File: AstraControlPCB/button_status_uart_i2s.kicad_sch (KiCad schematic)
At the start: 17 parts, among them CN7 4P JST ZH, CN8 4P JST ZH, CN9 JST_ZH_6PIN_1A_250V

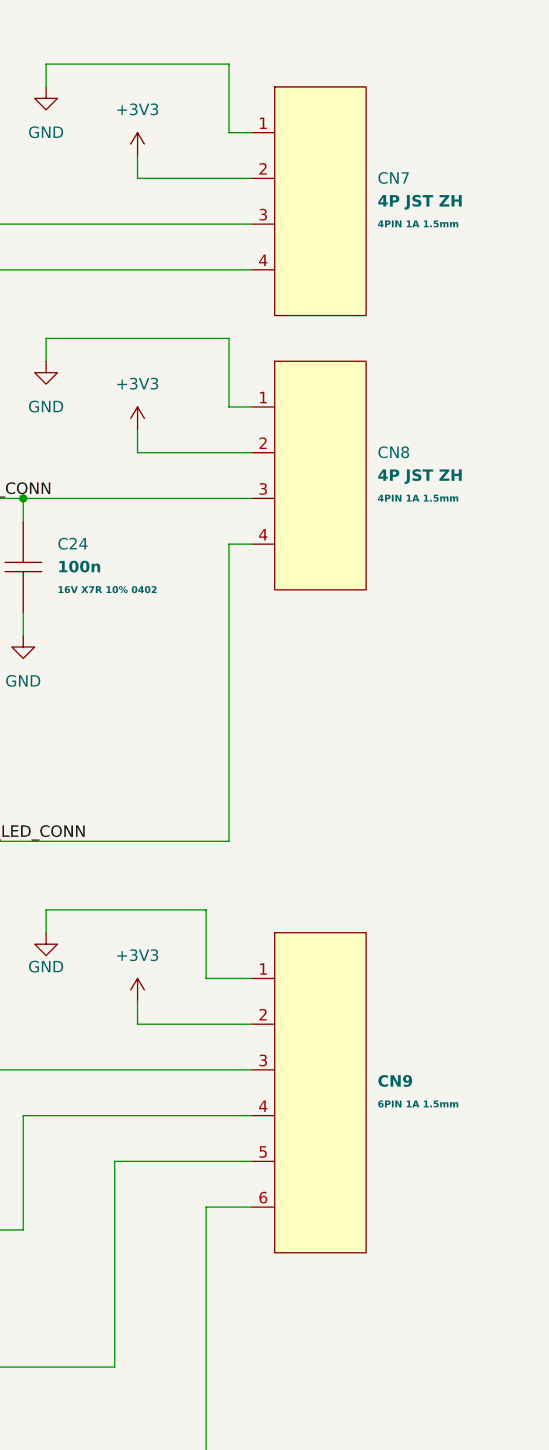
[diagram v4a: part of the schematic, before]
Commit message: Updated to JST SH, 3A diode for USB, added extra 2P VH
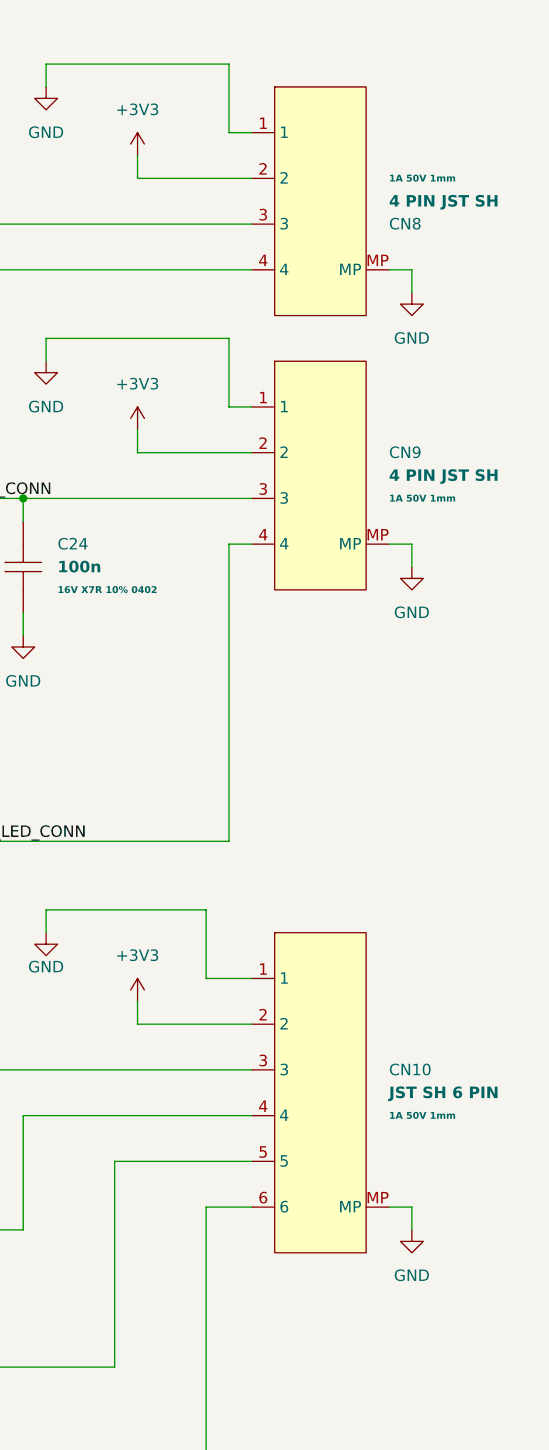
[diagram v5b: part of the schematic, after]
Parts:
- removed CN7, CN8: 4P JST ZH, LiveAstra:JST_ZH_B4B-ZR_1x04_P1.50mm_Vertical, symbol LiveAstra:JST_ZH_4PIN_1A_50V
- removed CN9: JST_ZH_6PIN_1A_250V, LiveAstra:JST_ZH_B6B-ZR_1x06_P1.50mm_Vertical, symbol LiveAstra:JST_ZH_6PIN_1A_250V
- added CN10: JST SH 6 PIN, LiveAstra:JST_SH_1x06_P1.00mm_Vertical, symbol LiveAstra:JST_SH_6PIN_1A_50V
- added CN8, CN9: 4 PIN JST SH, LiveAstra:JST_SH_1x04_P1.00mm_Vertical, symbol LiveAstra:JST_SH_4PIN_1A_50V
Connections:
- net +3V3: now also CN10.2, CN8.2, CN9.2
- net BUTTON_CONN: now also CN9.3
- net GND: now also CN10.1, CN10.MP, CN8.1, CN8.MP, CN9.1, CN9.MP
- net I2S_LR: now also CN10.6
- net I2S_SCK: now also CN10.4
- net I2S_SD: now also CN10.3
- net I2S_WS: now also CN10.5
- net STATUS_LED_CONN: now also CN9.4
- net UART_RX: now also CN8.4
- net UART_TX: now also CN8.3

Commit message: Update revision and add year to silkscreen
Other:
- title: AstraControl - HMI UART I2S -> AstraControl - Root
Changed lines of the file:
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@@
 	(paper "A4")
 	(title_block
-		(title "AstraControl - HMI UART I2S")
+		(title "AstraControl - Root")
 		(date "2024-08-26")
-		(rev "A")
+		(rev "B")
 		(company "LiveAstra Technologies")
 	)

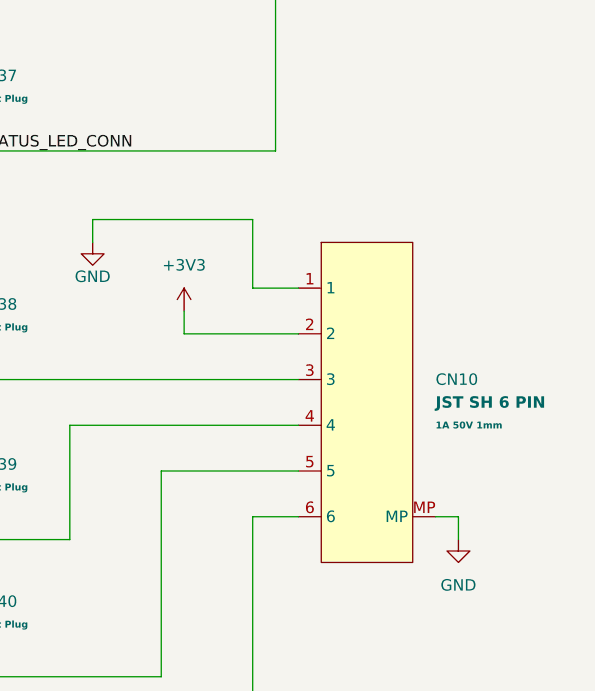
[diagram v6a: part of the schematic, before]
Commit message: Use alternative sh 6 pin that is in stock
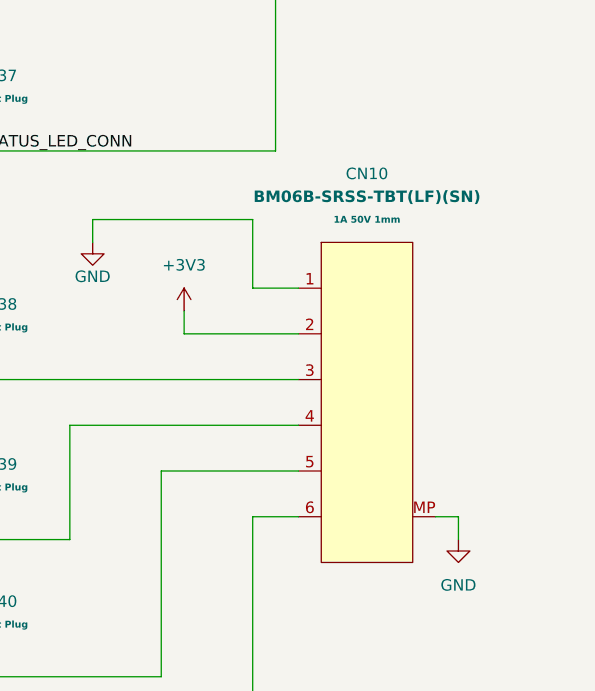
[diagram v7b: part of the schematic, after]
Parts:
- removed CN10: JST SH 6 PIN, LiveAstra:JST_SH_1x06_P1.00mm_Vertical, symbol LiveAstra:JST_SH_6PIN_1A_50V
- added CN10: BM06B-SRSS-TBT(LF)(SN), LiveAstra:JST_SH_1x06_P1.00mm_SMD_Vertical, symbol LiveAstra:JST_SH_6PIN_SMD_1A_50V
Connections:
- net +3V3: now also CN10.2
- net GND: now also CN10.1, CN10.MP
- net I2S_LR: now also CN10.6
- net I2S_SCK: now also CN10.4
- net I2S_SD: now also CN10.3
- net I2S_WS: now also CN10.5
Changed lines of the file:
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@@
 	)
 	(symbol
-		(lib_id "LiveAstra:JST_SH_6PIN_1A_50V")
+		(lib_id "LiveAstra:JST_SH_6PIN_SMD_1A_50V")
 		(at 182.88 134.62 0)
 		(unit 1)
@@
 		(on_board yes)
 		(dnp no)
+		(fields_autoplaced yes)
 		(property "Reference" "CN10"
-			(at 190.5 132.08 0)
+			(at 182.88 109.22 0)
 			(effects
 				(font
 					(size 1.27 1.27)
 				)
-				(justify left)
 			)
 		)
-		(property "Value" "JST SH 6 PIN"
-			(at 190.5 134.62 0)
+		(property "Value" "BM06B-SRSS-TBT(LF)(SN)"
+			(at 182.88 111.76 0)
 			(effects
 				(font
@@
 					(bold yes)
 				)
-				(justify left)
 			)
 		)
-		(property "Footprint" "LiveAstra:JST_SH_1x06_P1.00mm_Vertical"
-			(at 182.88 156.21 0)
-			(effects
-				(font
-					(size 1.27 1.27)
-				)
-				(hide yes)
-			)
-		)
-		(property "Datasheet" "https://lcsc.com/product-detail/Others_JST-Sales-America__JST-Sales-America-BM06B-SRSS-TB-LF-SN_C160392.html"
+		(property "Footprint" "LiveAstra:JST_SH_1x06_P1.00mm_SMD_Vertical"
 			(at 182.88 160.02 0)
 			(effects
@@
 			)
 		)
-		(property "Description" "1x6P 6P SH Tin 6 -25℃~+85℃ 1A 1 1mm Brass Alloy Standing paste SMD,P=1mm Wire To Board Connector ROHS"
-			(at 182.88 167.64 0)
+		(property "Datasheet" "https://lcsc.com/product-detail/New-Arrivals_JST-Sales-America-BM06B-SRSS-TBT-LF-SN_C495540.html"
+			(at 182.88 165.1 0)
 			(effects
 				(font
@@
 			)
 		)
-		(property "LCSC Part" "C160392"
-			(at 182.88 163.83 0)
+		(property "Description" "1x6P 6P SH Tin 6 -25℃~+85℃ 1A 1 1mm Brass Alloy Standing paste SMD,P=1mm Wire To Board Connector ROHS"
+			(at 182.88 175.26 0)
+			(effects
+				(font
+					(size 1.27 1.27)
+				)
+				(hide yes)
+			)
+		)
+		(property "LCSC Part" "C495540"
+			(at 182.88 154.94 0)
 			(effects
 				(font
@@
 		)
 		(property "Extra Values" "1A 50V 1mm"
-			(at 190.5 137.16 0)
+			(at 182.88 114.3 0)
 			(effects
 				(font
@@
 					(bold yes)
 				)
-				(justify left)
 			)
 		)
-		(property "MFR" "JST"
-			(at 182.88 175.26 0)
+		(property "MFN" "JST"
+			(at 182.88 180.34 0)
 			(effects
 				(font
@@
 			)
 		)
-		(property "MPN" "BM06B-SRSS-TB(LF)(SN)"
-			(at 182.88 171.45 0)
+		(property "MPN" "BM06B-SRSS-TBT(LF)(SN)"
+			(at 182.88 170.18 0)
 			(effects
 				(font
@@
 			)
 		)
+		(pin "6"
+		)
+		(pin "2"
+		)
+		(pin "MP"
+		)
 		(pin "1"
 		)
 		(pin "4"
 		)
-		(pin "MP"
+		(pin "5"
 		)
 		(pin "3"
 		)
-		(pin "6"
-		)
-		(pin "5"
-		)
-		(pin "2"
-		)
 		(instances
-			(project ""
+			(project "AstraControl"
 				(path "/9a751838-dce8-4d69-8a02-736625ac74e7/0db21d8e-3390-4d67-877f-0e5d98e37848/457d2566-de00-4e8c-b469-a22ed41e6193"
 					(reference "CN10")

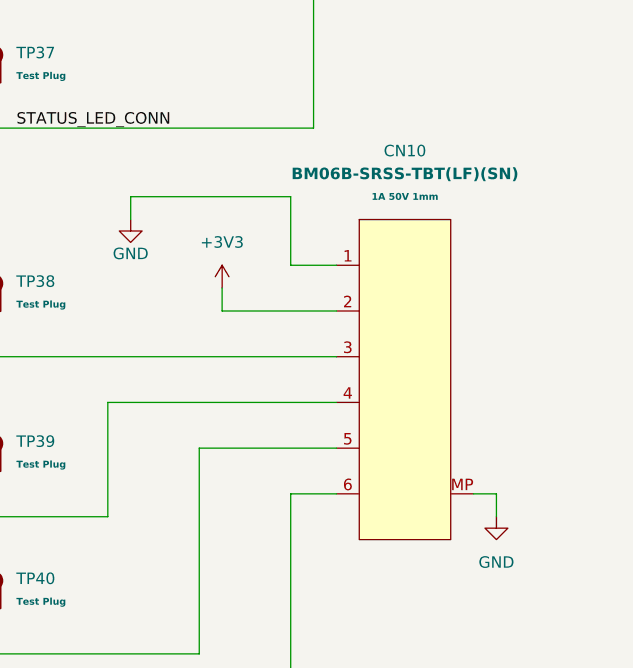
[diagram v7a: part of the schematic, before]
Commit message: Revert to normal jst connector without solder retention cup
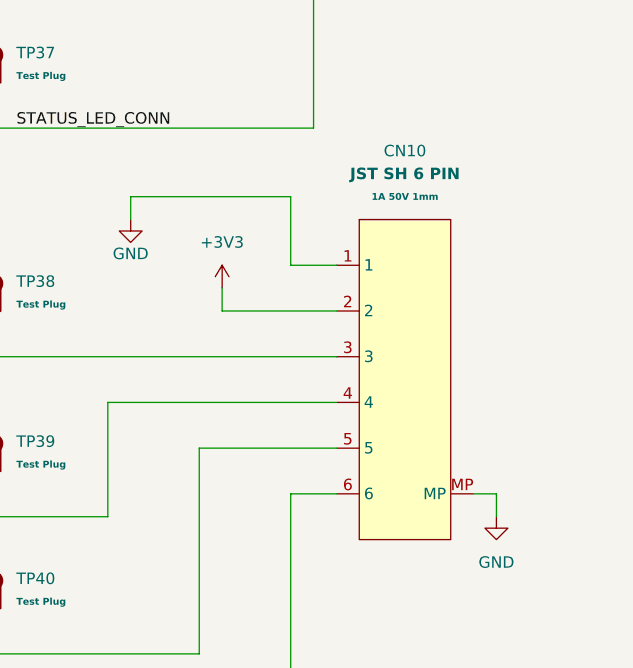
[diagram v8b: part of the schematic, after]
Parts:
- removed CN10: BM06B-SRSS-TBT(LF)(SN), LiveAstra:JST_SH_1x06_P1.00mm_SMD_Vertical, symbol LiveAstra:JST_SH_6PIN_SMD_1A_50V
- added CN10: JST SH 6 PIN, LiveAstra:JST_SH_1x06_P1.00mm_Vertical, symbol LiveAstra:JST_SH_6PIN_1A_50V
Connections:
- net +3V3: now also CN10.2
- net GND: now also CN10.1, CN10.MP
- net I2S_LR: now also CN10.6
- net I2S_SCK: now also CN10.4
- net I2S_SD: now also CN10.3
- net I2S_WS: now also CN10.5
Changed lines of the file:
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@@
-	)
-	(symbol
-		(lib_id "LiveAstra:JST_SH_6PIN_SMD_1A_50V")
-		(at 182.88 134.62 0)
-		(unit 1)
-		(exclude_from_sim no)
-		(in_bom yes)
-		(on_board yes)
-		(dnp no)
-		(fields_autoplaced yes)
-		(property "Reference" "CN10"
-			(at 182.88 109.22 0)
-			(effects
-				(font
-					(size 1.27 1.27)
-				)
-			)
-		)
-		(property "Value" "BM06B-SRSS-TBT(LF)(SN)"
-			(at 182.88 111.76 0)
-			(effects
-				(font
-					(size 1.27 1.27)
-					(bold yes)
-				)
-			)
-		)
-		(property "Footprint" "LiveAstra:JST_SH_1x06_P1.00mm_SMD_Vertical"
-			(at 182.88 160.02 0)
-			(effects
-				(font
-					(size 1.27 1.27)
-				)
-				(hide yes)
-			)
-		)
-		(property "Datasheet" "https://lcsc.com/product-detail/New-Arrivals_JST-Sales-America-BM06B-SRSS-TBT-LF-SN_C495540.html"
-			(at 182.88 165.1 0)
-			(effects
-				(font
-					(size 1.27 1.27)
-				)
-				(hide yes)
-			)
-		)
-		(property "Description" "1x6P 6P SH Tin 6 -25℃~+85℃ 1A 1 1mm Brass Alloy Standing paste SMD,P=1mm Wire To Board Connector ROHS"
-			(at 182.88 175.26 0)
-			(effects
-				(font
-					(size 1.27 1.27)
-				)
-				(hide yes)
-			)
-		)
-		(property "LCSC Part" "C495540"
-			(at 182.88 154.94 0)
-			(effects
-				(font
-					(size 1.27 1.27)
-				)
-				(hide yes)
-			)
-		)
-		(property "Extra Values" "1A 50V 1mm"
-			(at 182.88 114.3 0)
-			(effects
-				(font
-					(size 0.762 0.762)
-					(bold yes)
-				)
-			)
-		)
-		(property "MFN" "JST"
-			(at 182.88 180.34 0)
-			(effects
-				(font
-					(size 1.27 1.27)
-				)
-				(hide yes)
-			)
-		)
-		(property "MPN" "BM06B-SRSS-TBT(LF)(SN)"
-			(at 182.88 170.18 0)
-			(effects
-				(font
-					(size 1.27 1.27)
-				)
-				(hide yes)
-			)
-		)
-		(pin "6"
-		)
-		(pin "2"
-		)
-		(pin "MP"
-		)
-		(pin "1"
-		)
-		(pin "4"
-		)
-		(pin "5"
-		)
-		(pin "3"
-		)
-		(instances
-			(project "AstraControl"
-				(path "/9a751838-dce8-4d69-8a02-736625ac74e7/0db21d8e-3390-4d67-877f-0e5d98e37848/457d2566-de00-4e8c-b469-a22ed41e6193"
-					(reference "CN10")
-					(unit 1)
-				)
-			)
-		)
 	)
 	(symbol
@@
 					(unit 1)
 				)
+			)
+		)
+	)
+	(symbol
+		(lib_id "LiveAstra:JST_SH_6PIN_1A_50V")
+		(at 182.88 134.62 0)
+		(unit 1)
+		(exclude_from_sim no)
+		(in_bom yes)
+		(on_board yes)
+		(dnp no)
+		(fields_autoplaced yes)
+		(property "Reference" "CN10"
+			(at 182.88 109.22 0)
+			(effects
+				(font
+					(size 1.27 1.27)
+				)
+			)
+		)
+		(property "Value" "JST SH 6 PIN"
+			(at 182.88 111.76 0)
+			(effects
+				(font
+					(size 1.27 1.27)
+					(bold yes)
+				)
+			)
+		)
+		(property "Footprint" "LiveAstra:JST_SH_1x06_P1.00mm_Vertical"
+			(at 182.88 156.21 0)
+			(effects
+				(font
+					(size 1.27 1.27)
+				)
+				(hide yes)
+			)
+		)
+		(property "Datasheet" "https://lcsc.com/product-detail/Others_JST-Sales-America__JST-Sales-America-BM06B-SRSS-TB-LF-SN_C160392.html"
+			(at 182.88 160.02 0)
+			(effects
+				(font
+					(size 1.27 1.27)
+				)
+				(hide yes)
+			)
+		)
+		(property "Description" "1x6P 6P SH Tin 6 -25℃~+85℃ 1A 1 1mm Brass Alloy Standing paste SMD,P=1mm Wire To Board Connector ROHS"
+			(at 182.88 167.64 0)
+			(effects
+				(font
+					(size 1.27 1.27)
+				)
+				(hide yes)
+			)
+		)
+		(property "LCSC Part" "C160392"
+			(at 182.88 163.83 0)
+			(effects
+				(font
+					(size 1.27 1.27)
+				)
+				(hide yes)
+			)
+		)
+		(property "Extra Values" "1A 50V 1mm"
+			(at 182.88 114.3 0)
+			(effects
+				(font
+					(size 0.762 0.762)
+					(bold yes)
+				)
+			)
+		)
+		(property "MFR" "JST"
+			(at 182.88 175.26 0)
+			(effects
+				(font
+					(size 1.27 1.27)
+				)
+				(hide yes)
+			)
+		)
+		(property "MPN" "BM06B-SRSS-TB(LF)(SN)"
+			(at 182.88 171.45 0)
+			(effects
+				(font
+					(size 1.27 1.27)
+				)
+				(hide yes)
+			)
+		)
+		(pin "6"
+		)
+		(pin "1"
+		)
+		(pin "MP"
+		)
+		(pin "3"
+		)
+		(pin "4"
+		)
+		(pin "2"
+		)
+		(pin "5"
+		)
+		(instances
+			(project ""
+				(path "/9a751838-dce8-4d69-8a02-736625ac74e7/0db21d8e-3390-4d67-877f-0e5d98e37848/457d2566-de00-4e8c-b469-a22ed41e6193"
+					(reference "CN10")
+					(unit 1)
+				)
